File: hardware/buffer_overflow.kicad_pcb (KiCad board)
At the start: 2 copper layers, 33.1 x 30.1 mm, 19 parts, among them J1 E1, U1 LM741

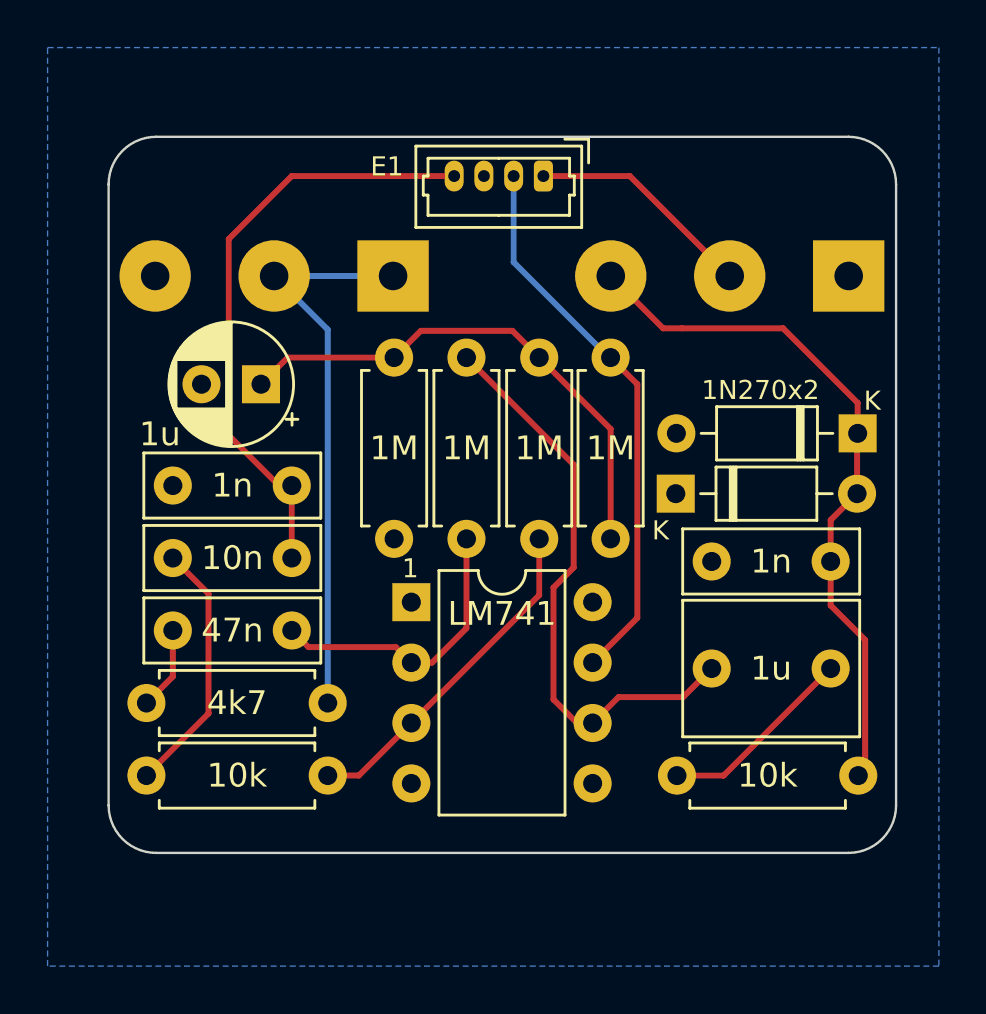
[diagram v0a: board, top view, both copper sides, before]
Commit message: v0.40 - proof-of-concept for Noise Floor UX board
 - change to SMD resistors and capacitors
 - full re-layout and re-route to accomodate board-to-board assemblies
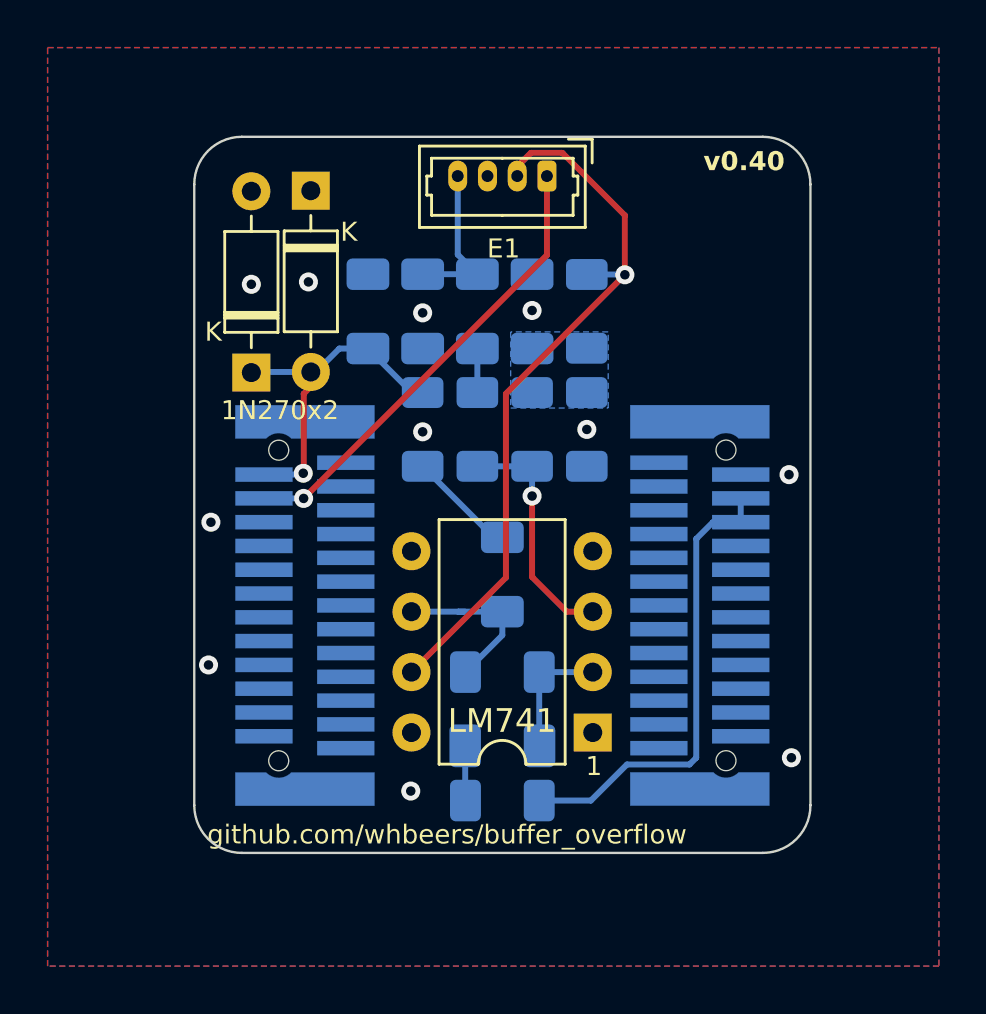
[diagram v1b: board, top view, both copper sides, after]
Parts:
- removed POT1: A10k, buffer_overflow:Potentiometer_Single_3_Horizontal
- removed POT2: B1M, buffer_overflow:Potentiometer_Single_3_Horizontal
- added J2: UX1, buffer_overflow:Amphenol_Header_25Pin_10162582-1134125LF, B.Cu at (53.4, 47.3)
- added J3: UX2, buffer_overflow:Amphenol_Header_25Pin_10162582-1134125LF, B.Cu at (70.0, 47.3)
- C1, C3, C4, C7: footprint Capacitor_THT:C_Rect_L7.2mm_W2.5mm_P5.00mm_FKS2_FKP2_MKS2_MKP2 -> Capacitor_SMD:C_1206_3216Metric_Pad1.33x1.80mm_HandSolder; moved to B.Cu
- C5: footprint Capacitor_THT:CP_Radial_D5.0mm_P2.50mm -> Capacitor_SMD:C_1206_3216Metric_Pad1.33x1.80mm_HandSolder; moved to B.Cu
- C6: footprint Capacitor_THT:C_Rect_L7.2mm_W5.5mm_P5.00mm_FKS2_FKP2_MKS2_MKP2 -> Capacitor_SMD:C_1206_3216Metric_Pad1.33x1.80mm_HandSolder; moved to B.Cu
- R2, R3, R4, R5, R6, R7, R8: footprint Resistor_THT:R_Axial_DIN0207_L6.3mm_D2.5mm_P7.62mm_Horizontal -> Resistor_SMD:R_1206_3216Metric_Pad1.30x1.75mm_HandSolder; moved to B.Cu
- moved D4 25.6 mm to (51.1, 37.5), turned to 90 degrees
- moved R8 23.4 mm to (58.3, 39.9), turned to -90 degrees
- moved R2 20.1 mm to (60.6, 39.9), turned to -90 degrees
- moved D3 19.9 mm to (53.6, 29.9), turned to -90 degrees
- moved C7 17.9 mm to (56.0, 34.9), turned to -90 degrees
- moved R6 15.5 mm to (61.6, 55.5)
- moved C4 14.7 mm to (61.6, 53.2)
- moved R7 13.3 mm to (61.6, 50.1), turned to 0 degrees
- moved C3 13.0 mm to (60.6, 34.9), turned to -90 degrees
- moved C1 12.8 mm to (58.3, 34.9), turned to 90 degrees
- moved C5 11.8 mm to (62.9, 34.9), turned to 90 degrees
- moved C6 9.65 mm to (61.6, 46.0), turned to 90 degrees
- moved R4 9.61 mm to (65.2, 34.9)
- moved U1 9.39 mm to (65.5, 52.6), turned to 180 degrees
- moved R5 9.32 mm to (65.2, 39.9)
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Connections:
- net /PRE_VOLUME renamed /POT3_CCW
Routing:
- net /VREF: track 22.0 -> 0.00 mm
- net /EFFECT_IN: track 25.4 -> 6.77 mm
- net /741_OUT: track 24.6 -> 7.30 mm
- net /POT3_CCW: track 29.5 -> 14.4 mm, vias 0 -> 1
- net /EFFECT_OUT: track 9.57 -> 19.5 mm, vias 0 -> 1
- net Net-(C3-Pad2): track 10.8 -> 1.85 mm
- net /9V0: track 23.4 -> 30.8 mm, vias 0 -> 1
- net /741_Inv: track 12.3 -> 5.36 mm
- net /741_NonInv: track 14.4 -> 10.1 mm, vias 0 -> 1
- net /GAIN_CTL: track 23.9 -> 19.7 mm
- net Net-(C6-Pad2): track 8.32 -> 4.59 mm
- net Net-(C4-Pad1): track 3.51 -> 2.31 mm
- net GND: vias 0 -> 11
- added copper zone on B.Cu, net /VREF
- added copper zone on F.Cu, net GND
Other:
- board size 33.1 x 30.1 mm -> 25.9 x 30.1 mm
- board text added: "${COMMENT1}"
- board text added: "${REVISION}"
- board text removed: "${COMMENT1} ${REVISION}"

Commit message: Fix issue detected in hardware version v0.40
 - swap backwards volume knob pins
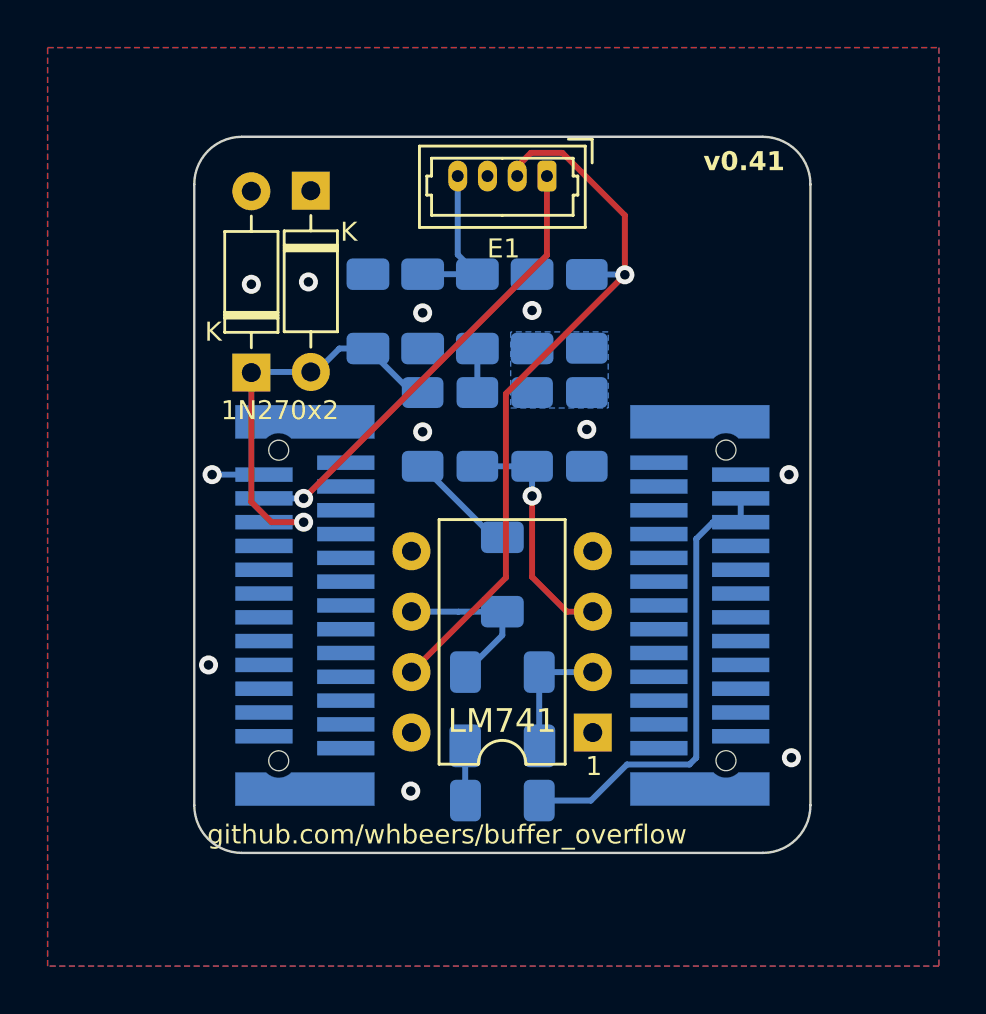
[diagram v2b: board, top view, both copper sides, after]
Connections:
- C7 pad 2: /POT3_CCW -> /POT3_CW
- D3 pad 2: /POT3_CCW -> /POT3_CW
- D4 pad 1: /POT3_CCW -> /POT3_CW
- J2 pad 23: GND -> /POT3_CW
- J2 pad 25: /POT3_CCW -> GND
- R8 pad 1: /POT3_CCW -> /POT3_CW
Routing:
- net /POT3_CW: track 0.00 -> 18.0 mm, vias 0 -> 1
- net /POT3_CCW: track 14.4 -> 0.00 mm, vias 1 -> 0
- net GND: track 0.00 -> 2.18 mm
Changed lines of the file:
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@@
   (title_block
     (title "Buffer Overflow Drive Effect")
-    (date "2023-03-27")
-    (rev "v0.40")
+    (date "2023-04-16")
+    (rev "v0.41")
     (comment 1 " github.com/whbeers/buffer_overflow")
   )
@@
   (net 34 "unconnected-(J2-Pin_19-Pad19)")
   (net 35 "unconnected-(J2-Pin_22-Pad22)")
-  (net 36 "/POT3_CCW")
+  (net 36 "/POT3_CW")
   (net 37 "unconnected-(J3-Pin_1-Pad1)")
   (net 38 "unconnected-(J3-Pin_2-Pad2)")
@@
       (net 1 "GND") (pinfunction "K") (pintype "passive"))
     (pad "2" thru_hole oval (at 7.62 0 270) (size 1.6 1.6) (drill 0.8) (layers "*.Cu" "*.Mask")
-      (net 36 "/POT3_CCW") (pinfunction "A") (pintype "passive"))
+      (net 36 "/POT3_CW") (pinfunction "A") (pintype "passive"))
     (model "${KICAD6_3DMODEL_DIR}/Diode_THT.3dshapes/D_DO-35_SOD27_P7.62mm_Horizontal.wrl"
       (offset (xyz 0 0 0))
@@
       (stroke (width 0.1) (type solid)) (layer "F.Fab"))
     (pad "1" thru_hole rect (at 0 0 90) (size 1.6 1.6) (drill 0.8) (layers "*.Cu" "*.Mask")
-      (net 36 "/POT3_CCW") (pinfunction "K") (pintype "passive"))
+      (net 36 "/POT3_CW") (pinfunction "K") (pintype "passive"))
     (pad "2" thru_hole oval (at 7.62 0 90) (size 1.6 1.6) (drill 0.8) (layers "*.Cu" "*.Mask")
       (net 1 "GND") (pinfunction "A") (pintype "passive"))
@@
       (stroke (width 0.1) (type solid)) (layer "B.Fab"))
     (pad "1" smd roundrect (at -1.55 0 270) (size 1.3 1.75) (layers "B.Cu" "B.Paste" "B.Mask") (roundrect_rratio 0.192308)
-      (net 36 "/POT3_CCW") (pintype "passive"))
+      (net 36 "/POT3_CW") (pintype "passive"))
     (pad "2" smd roundrect (at 1.55 0 270) (size 1.3 1.75) (layers "B.Cu" "B.Paste" "B.Mask") (roundrect_rratio 0.192308)
       (net 4 "Net-(C6-Pad2)") (pintype "passive"))
@@
       (net 35 "unconnected-(J2-Pin_22-Pad22)") (pinfunction "Pin_22") (pintype "passive+no_connect"))
     (pad "23" smd rect (at 3.5 -1.72 90) (size 0.61 2.41) (layers "B.Cu" "B.Mask")
-      (net 1 "GND") (pinfunction "Pin_23") (pintype "passive"))
+      (net 36 "/POT3_CW") (pinfunction "Pin_23") (pintype "passive"))
     (pad "24" smd rect (at 4.5 -1.72 90) (size 0.61 2.41) (layers "B.Cu" "B.Mask")
       (net 12 "/EFFECT_OUT") (pinfunction "Pin_24") (pintype "passive"))
     (pad "25" smd rect (at 5.5 -1.72 90) (size 0.61 2.41) (layers "B.Cu" "B.Mask")
-      (net 36 "/POT3_CCW") (pinfunction "Pin_25") (pintype "passive"))
+      (net 1 "GND") (pinfunction "Pin_25") (pintype "passive"))
     (pad "S1" smd custom (at -7.72 0 90) (size 0.8 0.8) (layers "B.Cu")
       (zone_connect 0) (thermal_bridge_angle 45)
@@
       (net 1 "GND") (pintype "passive"))
     (pad "2" smd roundrect (at 1.5625 0 270) (size 1.325 1.8) (layers "B.Cu" "B.Paste" "B.Mask") (roundrect_rratio 0.188679)
-      (net 36 "/POT3_CCW") (pintype "passive"))
+      (net 36 "/POT3_CW") (pintype "passive"))
     (model "${KICAD6_3DMODEL_DIR}/Capacitor_SMD.3dshapes/C_1206_3216Metric.wrl"
       (offset (xyz 0 0 0))
@@
   (via (at 51.1 33.8) (size 0.8) (drill 0.4) (layers "F.Cu" "B.Cu") (free) (net 1))
   (via (at 49.3 49.8) (size 0.8) (drill 0.4) (layers "F.Cu" "B.Cu") (free) (net 1))
-  (via (at 49.4 43.8) (size 0.8) (drill 0.4) (layers "F.Cu" "B.Cu") (free) (net 1))
   (via (at 73.7 41.8) (size 0.8) (drill 0.4) (layers "F.Cu" "B.Cu") (free) (net 1))
   (via (at 58.3 35) (size 0.8) (drill 0.4) (layers "F.Cu" "B.Cu") (free) (net 1))
@@
   (via (at 73.8 53.7) (size 0.8) (drill 0.4) (layers "F.Cu" "B.Cu") (free) (net 1))
   (via (at 58.3 40) (size 0.8) (drill 0.4) (layers "F.Cu" "B.Cu") (free) (net 1))
+  (via (at 49.45 41.8) (size 0.8) (drill 0.4) (layers "F.Cu" "B.Cu") (net 1))
   (via (at 53.5 33.7) (size 0.8) (drill 0.4) (layers "F.Cu" "B.Cu") (free) (net 1))
-  (segment (start 51.628 43.8) (end 51.63 43.798) (width 0.25) (layer "B.Cu") (net 1))
+  (segment (start 49.452 41.798) (end 49.45 41.8) (width 0.25) (layer "B.Cu") (net 1))
+  (segment (start 51.63 41.798) (end 49.452 41.798) (width 0.25) (layer "B.Cu") (net 1))
   (segment (start 60.0875 53.2) (end 60.0875 55.4875) (width 0.25) (layer "B.Cu") (net 2))
   (segment (start 60.0875 55.4875) (end 60.1 55.5) (width 0.25) (layer "B.Cu") (net 2))
@@
   (segment (start 61.65 48.55) (end 60.1 50.1) (width 0.25) (layer "B.Cu") (net 8))
   (segment (start 59.8 47.56) (end 57.83 47.56) (width 0.25) (layer "B.Cu") (net 8))
-  (segment (start 60.1 47.56) (end 59.8 47.56) (width 0.25) (layer "B.Cu") (net 8))
   (segment (start 61.65 47.56) (end 59.8 47.56) (width 0.25) (layer "B.Cu") (net 8))
   (segment (start 65.37231 55.5) (end 66.88831 53.984) (width 0.25) (layer "B.Cu") (net 9))
@@
   (segment (start 51.631877 42.799877) (end 51.63 42.798) (width 0.25) (layer "B.Cu") (net 12))
   (segment (start 53.297457 42.799877) (end 51.631877 42.799877) (width 0.25) (layer "B.Cu") (net 12))
-  (segment (start 53.3 38.4) (end 53.6 38.1) (width 0.25) (layer "F.Cu") (net 36))
-  (segment (start 53.3 41.723376) (end 53.3 38.4) (width 0.25) (layer "F.Cu") (net 36))
-  (segment (start 53.6 38.1) (end 53.6 37.485) (width 0.25) (layer "F.Cu") (net 36))
-  (segment (start 53.281747 41.741629) (end 53.3 41.723376) (width 0.25) (layer "F.Cu") (net 36))
-  (via (at 53.281747 41.741629) (size 0.8) (drill 0.4) (layers "F.Cu" "B.Cu") (net 36))
+  (segment (start 51.1 37.51) (end 51.1 42.95) (width 0.25) (layer "F.Cu") (net 36))
+  (segment (start 51.949377 43.799377) (end 53.297627 43.799377) (width 0.25) (layer "F.Cu") (net 36))
+  (segment (start 51.1 42.95) (end 51.949377 43.799377) (width 0.25) (layer "F.Cu") (net 36))
+  (via (at 53.297627 43.799377) (size 0.8) (drill 0.4) (layers "F.Cu" "B.Cu") (net 36))
   (segment (start 56 36.5) (end 54.8 36.5) (width 0.25) (layer "B.Cu") (net 36))
   (segment (start 57.85 38.35) (end 56 36.5) (width 0.25) (layer "B.Cu") (net 36))
+  (segment (start 53.297627 43.799377) (end 51.631377 43.799377) (width 0.25) (layer "B.Cu") (net 36))
   (segment (start 51.125 37.485) (end 51.1 37.51) (width 0.25) (layer "B.Cu") (net 36))
   (segment (start 58.3 38.35) (end 57.85 38.35) (width 0.25) (layer "B.Cu") (net 36))
-  (segment (start 53.281747 41.741629) (end 53.225376 41.798) (width 0.25) (layer "B.Cu") (net 36))
-  (segment (start 53.225376 41.798) (end 51.63 41.798) (width 0.25) (layer "B.Cu") (net 36))
   (segment (start 53.815 37.485) (end 53.6 37.485) (width 0.25) (layer "B.Cu") (net 36))
   (segment (start 53.6 37.485) (end 51.125 37.485) (width 0.25) (layer "B.Cu") (net 36))
